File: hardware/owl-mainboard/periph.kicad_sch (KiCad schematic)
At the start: 0 parts

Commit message: feat(hardware): draw the display, sensor and dock sheet; main board ERC clean
The periph sheet carries J301 (FH26W-31S, connector pin k = panel pin
32 - k as on the Waveshare 1.75 kit J3) with a pin table aligned to the
connector pins, the panel decoupling and the touch bus pull-ups to
DISP_3V3, the DRV2605L on +3V3 with the LRA connector, the TMAG5273A2,
the LIS2DW12, the OPT3001, the sensor bus pull-ups, and the dock link
(J303, SMF5.0A, DOCK_DET divider with ESD). hw_netlist now runs in CI
for the main board.

One change to the planned parts: LIS2DW12 SDO/SA0 reaches +3V3 through
R309 10k (C25744, already on the board) on the new net IMU_SA0 instead
of a hard tie. The pin is an I/O (SPI SDO), and tying it to the
TPS63802 output was the only ERC violation (bidirectional pin on a power
output). ST's internal 20 to 30k SA0 pull-up is in parallel, so the
address stays 0x19.

Panel VBAT and touch I2C stay at 3.3 V as on the Waveshare kit (ruling
R18); the sheet and design.toml record the VIEWE pin table figures
(VBAT 3.7 to 4.5 V, touch I2C 1.8 V) as open bring-up items.

kicad-happy analyzer: 0 errors, 9 warnings, all judged false positives
or deliberate:
- RS-001 VBUS_USB and VBUS_DOCK have no declared source: both are fed
  by connectors (J201, J303) and carry no power_in pin; ERC is clean.
- PU-001 U101 TMR: left open on purpose (default safety timers).
- PU-001 U103 PG: pulled up through R212 4.7k and R205 47k on ESP_EN.
- PU-001 U104 QOD: tied to VOUT as TI specifies for quick discharge.
- PU-001 U303 INT2: push-pull output, unused and left open.
- UC-001 no capacitor on VBUS at J201: deliberate (ruling R35, C101
  4.7 uF sits behind D101).
- UC-002 no TVS on VBUS at J201: D201 SMF5.0A is there; the analyzer
  does not read a Zener-symbol TVS as one.
- DS-002 no datasheets directory: the datasheets were checked from
  local copies that are not committed.
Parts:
- added C301: 4.7uF, Capacitor_SMD:C_0402_1005Metric, symbol Device:C
- added C302, C305, C306, C307, C309, C310: 100nF, Capacitor_SMD:C_0402_1005Metric, symbol Device:C
- added C303, C304, C308: 1uF, Capacitor_SMD:C_0402_1005Metric, symbol Device:C
- added D301: SMF5.0A, Diode_SMD:D_SOD-123F, symbol Device:D_Zener
- added D302: LESD5D5.0CT1G, Diode_SMD:D_SOD-523, symbol Device:D_TVS
- added J301: AMOLED FPC, owltunes:Hirose_FH26W-31S-0.3SHW_1x31-1MP_P0.30mm_Horizontal, symbol Connector_Generic_MountingPin:Conn_01x31_MountingPin
- added J302: LRA, Connector_JST:JST_SH_SM02B-SRSS-TB_1x02-1MP_P1.00mm_Horizontal, symbol Connector_Generic_MountingPin:Conn_01x02_MountingPin
- added J303: DOCK: GND, VBUS, DET, GND, Connector_JST:JST_SH_SM04B-SRSS-TB_1x04-1MP_P1.00mm_Horizontal, symbol Connector_Generic_MountingPin:Conn_01x04_MountingPin
- added R301, R302, R305, R306: 4.7k, Resistor_SMD:R_0402_1005Metric, symbol Device:R
- added R303, R309: 10k, Resistor_SMD:R_0402_1005Metric, symbol Device:R
- added R304: 47k, Resistor_SMD:R_0402_1005Metric, symbol Device:R
- added R307: 1k, Resistor_SMD:R_0402_1005Metric, symbol Device:R
- added R308: 100k, Resistor_SMD:R_0402_1005Metric, symbol Device:R
- added U301: DRV2605LDGSR, Package_SO:TSSOP-10_3x3mm_P0.5mm, symbol Driver:DRV2605LDGS
- added U302: TMAG5273A2QDBVR, Package_TO_SOT_SMD:SOT-23-6, symbol owltunes:TMAG5273A2QDBVR
- added U303: LIS2DW12TR, Package_LGA:LGA-12_2x2mm_P0.5mm, symbol owltunes:LIS2DW12TR
- added U304: OPT3001DNPR, owltunes:TI_DNP_USON-6-1EP_2x2mm_P0.65mm, symbol owltunes:OPT3001DNPR
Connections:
- new net +3V3: C304.1, C305.1, C306.1, C307.1, C308.1, C309.1, R304.1, R305.1, R306.1, R308.1, R309.1, U301.10 (VDD), U301.5 (EN), U301.6 (VDD/NC), U302.4 (VCC), U303.10 (VDD_IO), U303.2 (CS), U303.9 (VDD), U304.1 (VDD)
- new net DISP_3V3: C301.1, C302.1, J301.21 (Pin_21), J301.22 (Pin_22), J301.23 (Pin_23), J301.24 (Pin_24), J301.26 (Pin_26), R301.1, R302.1, R303.1
- new net DOCK_DET: C310.1, R307.2, R308.2
- new net DOCK_PAD: D302.1 (A1), J303.3 (Pin_3), R307.1
- new net DRV_REG: C303.1, U301.1 (REG)
- new net GND: C301.2, C302.2, C303.2, C304.2, C305.2, C306.2, C307.2, C308.2, C309.2, C310.2, D301.2 (A), D302.2 (A2), J301.1 (Pin_1), J301.10 (Pin_10), J301.20 (Pin_20), J301.25 (Pin_25), J301.31 (Pin_31), J301.4 (Pin_4), J301.7 (Pin_7), J301.MP (MountPin), J302.MP (MountPin), J303.1 (Pin_1), J303.4 (Pin_4), J303.MP (MountPin), U301.4 (IN/TRIG), U301.8 (GND), U302.2 (GND), U302.3 (GND(TEST)), U303.6 (GND), U303.7 (RES), U303.8 (GND), U304.2 (ADDR), U304.3 (GND), U304.7 (EP)
- new net HALL_INT: R304.2, U302.5 (~{INT})
- new net I2C_SCL: R306.2, U301.2 (SCL), U302.1 (SCL), U303.1 (SCL/SPC), U304.4 (SCL)
- new net I2C_SDA: R305.2, U301.3 (SDA), U302.6 (SDA), U303.4 (SDA/SDI/SDO), U304.6 (SDA)
- new net IMU_INT1: U303.12 (INT1)
- new net IMU_SA0: R309.2, U303.3 (SDO/SA0)
- new net LCD_CLK: J301.14 (Pin_14)
- new net LCD_CS: J301.17 (Pin_17)
- new net LCD_D0: J301.16 (Pin_16)
- new net LCD_D1: J301.15 (Pin_15)
- new net LCD_D2: J301.12 (Pin_12)
- new net LCD_D3: J301.13 (Pin_13)
- new net LCD_RST: J301.18 (Pin_18)
- new net LCD_TE: J301.11 (Pin_11)
- new net LRA_N: J302.2 (Pin_2), U301.9 (OUT-)
- new net LRA_P: J302.1 (Pin_1), U301.7 (OUT+)
- new net TP_INT: J301.30 (Pin_30), R303.2
- new net TP_RST: J301.29 (Pin_29)
- new net TP_SCL: J301.27 (Pin_27), R302.2
- new net TP_SDA: J301.28 (Pin_28), R301.2
- new net VBUS_DOCK: D301.1 (K), J303.2 (Pin_2)
- no-connect marks 0 -> 10
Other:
- note added: "Ambient light sensor OPT3001 (0x44), behind the brow window"
- note added: "Connector pin k = panel pin 32 - k (Waveshare ESP32-S3-Touch-AMOLED-1.75 J3); bottom-contact FH26W, FPC contacts face the board"
- note added: "DOCK_DET = 3.3 V x (1k + 10k) / (100k + 1k + 10k) = 0.33 V on the perch (10k ID resistor there), 3.3 V undocked, 0.03 V with the pad shorted to GND. J303 is pin for pin with the dock-pad board."
- note added: "Display FPC (J301): panel supplies on DISP_3V3, touch bus pull-ups to DISP_3V3"
- note added: "Dock link (J303 to the dock-pad board): VBUS TVS, DOCK_DET divider with ESD"
- note added: "Haptics: DRV2605L on +3V3 (I2C0, 0x5A), EN tied high, LRA on J302"
- note added: "LRA Leader LD0832AA-0099F (off board): 8 mm, 1.8 V rms, 235 Hz, 24 ohm; leads crimped into a JST SH 2-pin housing"
- note added: "Ring sensor TMAG5273A2 (0x35) and accelerometer LIS2DW12 (0x19) on the sensor bus"
- note added: "Sensor bus pull-ups (I2C0) and SA0"

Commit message: fix(hardware): set the JLC rotation offsets the EasyEDA footprints call for
Each assembled part's EasyEDA footprint (JLC's placement zero) was matched pad by pad with
the KiCad footprint on the board. The Fabrication Toolkit writes a bottom rotation as 180
minus the KiCad rotation (the rotation seen from below, board turned over left to right,
true for all 81 bottom parts) plus its own table rotation, so a part needs the
EasyEDA-to-KiCad angle less the table's angle. Five parts get an FT Rotation Offset:

- D101, D102 (PMEG2020EH, C456104): 180. EasyEDA's footprint has pad 1, the cathode, on
  the right at zero; KiCad's D_SOD-123F has it on the left. No toolkit rule. CPL 180 -> 0.
- J101 (S2B-PH-SM4-TB, C295747): 180. EasyEDA's footprint matches KiCad's at zero; the
  toolkit's ^JST_PH_S rule adds 180, which this cancels. CPL 270 -> 90.
- U202 (USBLC6-2SC6, C7519): 90. EasyEDA's SOT-23-6 BL footprint (pin 1 bottom left, rows
  horizontal) is 270 from KiCad's; the toolkit's ^SOT-23 rule gives 180. CPL 180 -> 270.
- U303 (LIS2DW12TR, C189624): 270. EasyEDA's LGA-12 BL footprint runs pins 1 to 4 along
  the bottom, KiCad's down the left (ruling R30); no toolkit rule. CPL 180 -> 90.

The offsets live in design.toml (rotation_offset) and on the symbols; hw_sync.py now copies
the field to the footprint, where the toolkit reads it, hw_bom.py checks symbol against
design.toml and a test checks footprint against design.toml. JLC's placement preview
confirms them at order time. ordering.md and the review record the offsets and the method.

ERC 0, DRC 0/0/0 with parity, hw_fab 0 errors (top 6, bottom 81), Gerbers unchanged.
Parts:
- U303: FT Rotation Offset (none) -> 270
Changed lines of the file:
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@@
+			)
+		)
+		(property "FT Rotation Offset" "270"
+			(at 304.8 116.84 0)
+			(hide yes)
+			(show_name no)
+			(do_not_autoplace no)
+			(effects
+				(font
+					(size 1.27 1.27)
+				)
 			)
 		)

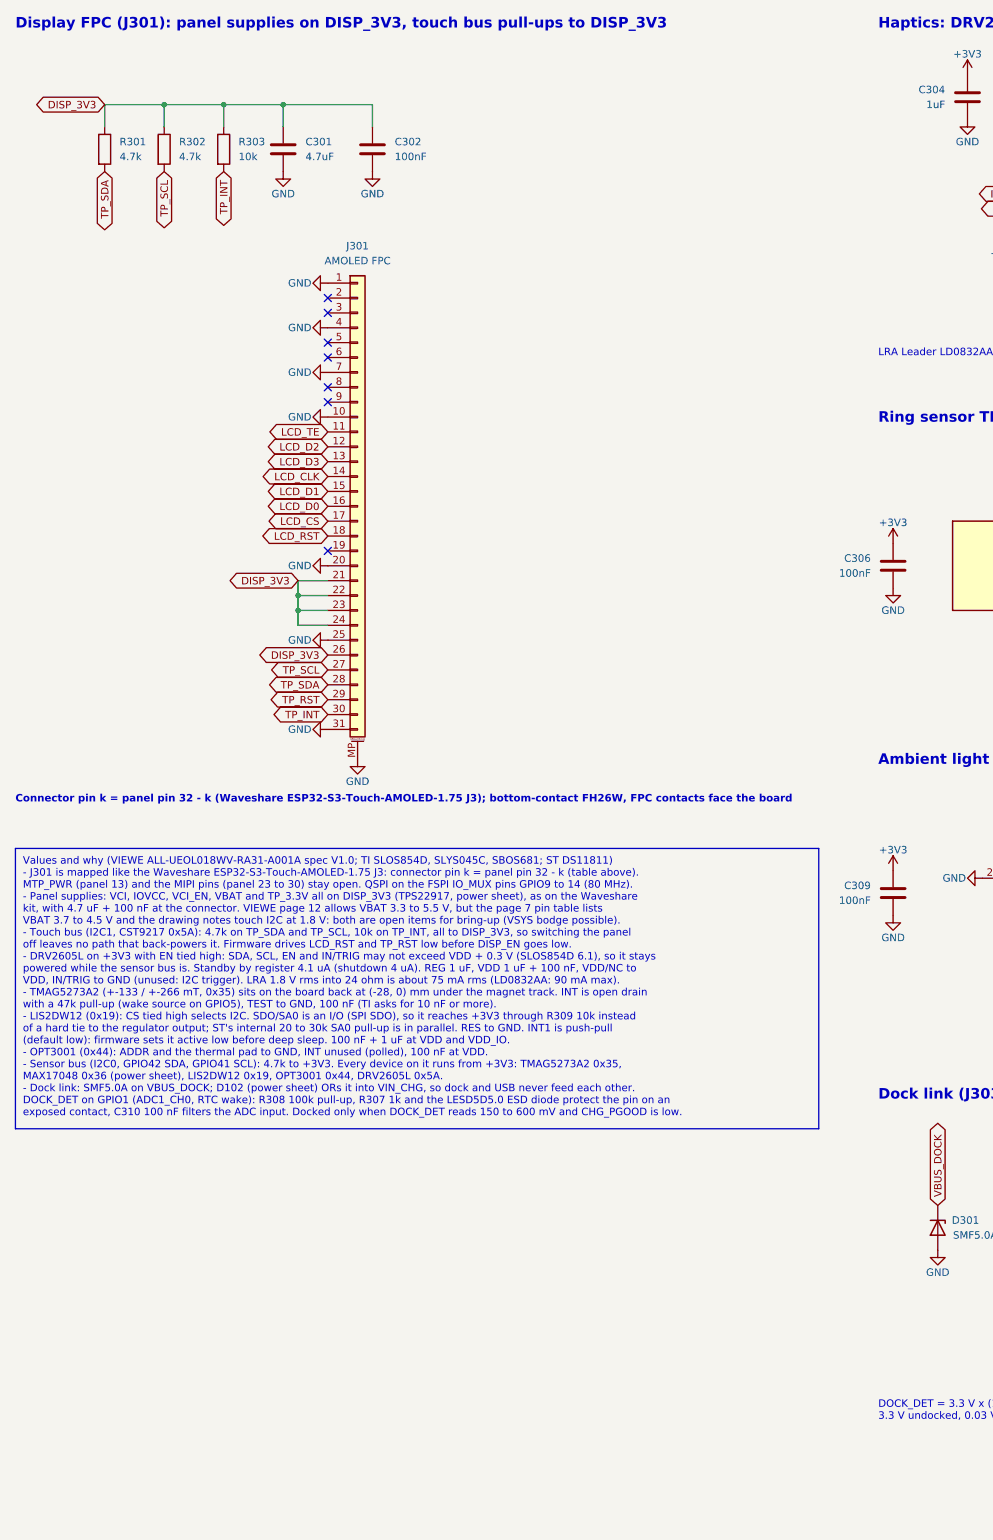
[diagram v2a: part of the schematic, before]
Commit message: feat(hardware): draw the touch level shift on the periph sheet
U305 (LSF0204PWR) and U306 (XC6206P182MR) with C311, C312, R310 and the
1.8 V pull-ups R311 to R314 go below the J301 notes, as in design.toml.
J301 pins 27 to 30 now carry TP_SCL_1V8, TP_SDA_1V8, TP_RST_1V8 and
TP_INT_1V8; TP_* stay on U201, R301 to R303 and U305's B side. R315
(0R, the fallback to a 3.3 V touch bus) is drawn across U306 and marked
DNP, out of the BOM and the position files.

The J301 table, the "Values and why" box and the GPIO table on mcu_usb
now name the CST820 (0x15), the VIEWE V1.1 spec, the 40 MHz QSPI clock
and the touch lines' path through U305 at 1.8 V.
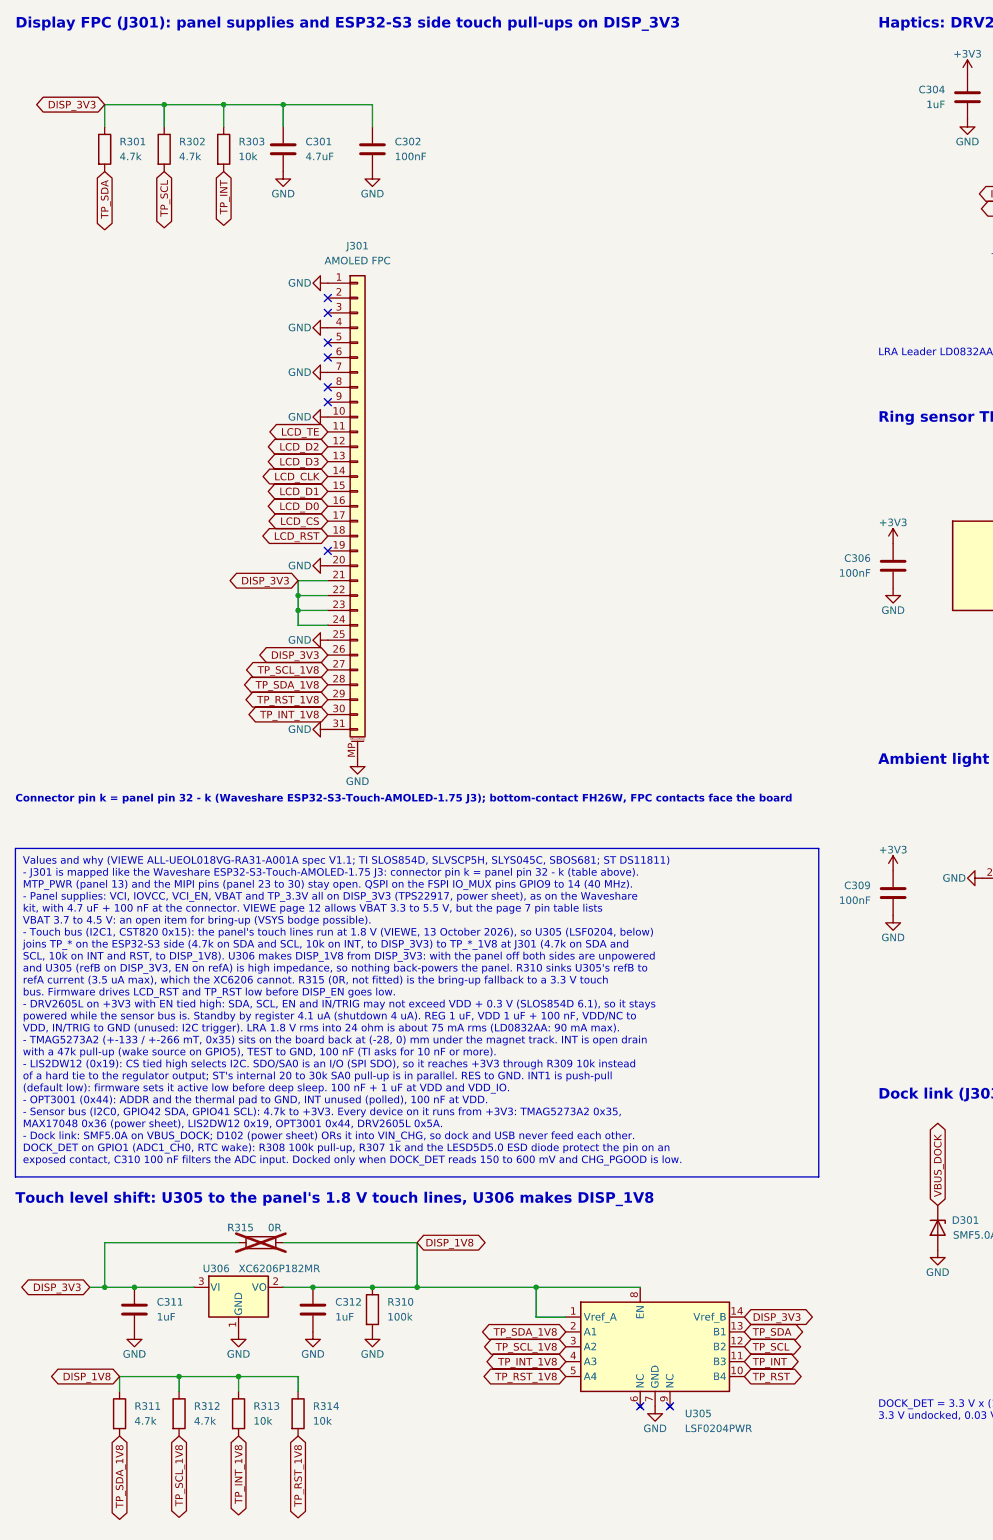
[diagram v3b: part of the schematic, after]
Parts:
- added C311, C312: 1uF, Capacitor_SMD:C_0402_1005Metric, symbol Device:C
- added R310: 100k, Resistor_SMD:R_0402_1005Metric, symbol Device:R
- added R311, R312: 4.7k, Resistor_SMD:R_0402_1005Metric, symbol Device:R
- added R313, R314: 10k, Resistor_SMD:R_0402_1005Metric, symbol Device:R
- added R315: 0R, Resistor_SMD:R_0402_1005Metric, symbol Device:R
- added U305: LSF0204PWR, Package_SO:TSSOP-14_4.4x5mm_P0.65mm, symbol owltunes:LSF0204PWR
- added U306: XC6206P182MR, Package_TO_SOT_SMD:SOT-23-3, symbol Regulator_Linear:XC6206PxxxMR
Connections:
- net DISP_3V3: now also C311.1, R315.1, U305.14 (Vref_B), U306.3 (VI)
- net GND: now also C311.2, C312.2, R310.2, U305.7 (GND), U306.1 (GND)
- net TP_INT: now also U305.11 (B3); no longer J301.30 (Pin_30)
- net TP_RST: now also U305.10 (B4); no longer J301.29 (Pin_29)
- net TP_SCL: now also U305.12 (B2); no longer J301.27 (Pin_27)
- net TP_SDA: now also U305.13 (B1); no longer J301.28 (Pin_28)
- new net DISP_1V8: C312.1, R310.1, R311.1, R312.1, R313.1, R314.1, R315.2, U305.1 (Vref_A), U305.8 (EN), U306.2 (VO)
- new net TP_INT_1V8: J301.30 (Pin_30), R313.2, U305.4 (A3)
- new net TP_RST_1V8: J301.29 (Pin_29), R314.2, U305.5 (A4)
- new net TP_SCL_1V8: J301.27 (Pin_27), R312.2, U305.3 (A2)
- new net TP_SDA_1V8: J301.28 (Pin_28), R311.2, U305.2 (A1)
- no-connect marks 10 -> 12
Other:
- note added: "Display FPC (J301): panel supplies and ESP32-S3 side touch pull-ups on DISP_3V3"
- note added: "Touch level shift: U305 to the panel's 1.8 V touch lines, U306 makes DISP_1V8"
- note removed: "Display FPC (J301): panel supplies on DISP_3V3, touch bus pull-ups to DISP_3V3"
